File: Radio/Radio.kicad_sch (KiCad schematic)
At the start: 22 parts, among them SW1 Bourns PEC11R, SW2 Bourns PEC11R, SW3 SW_Push, SW4 SW_Push, U1 LM386, U2 RDA5807M_Module

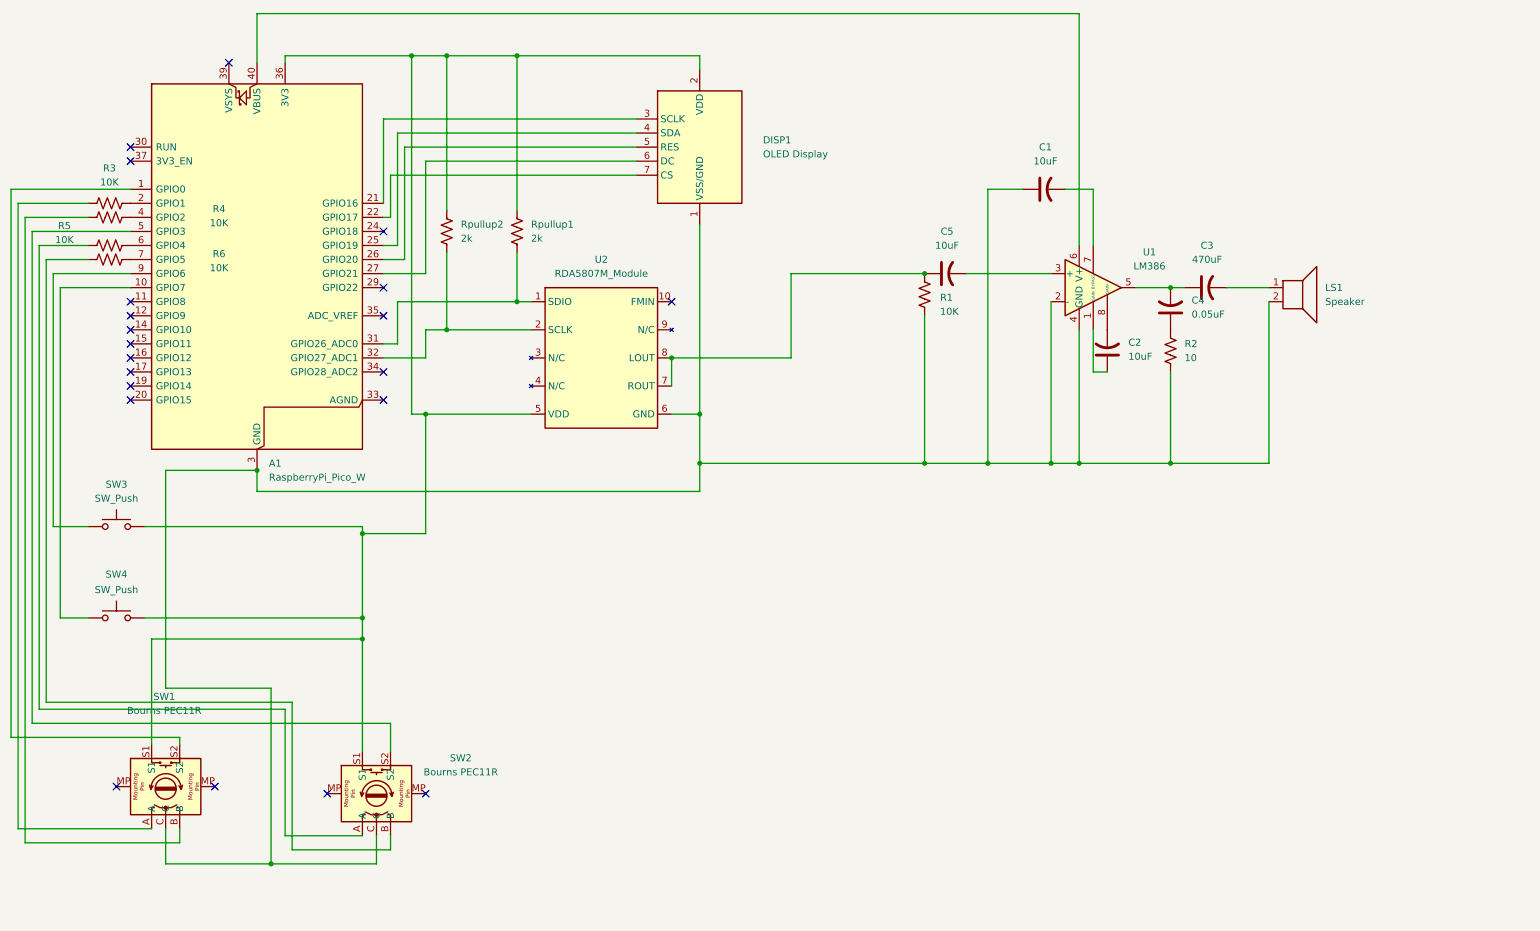
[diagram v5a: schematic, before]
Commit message: updated PCB with filters
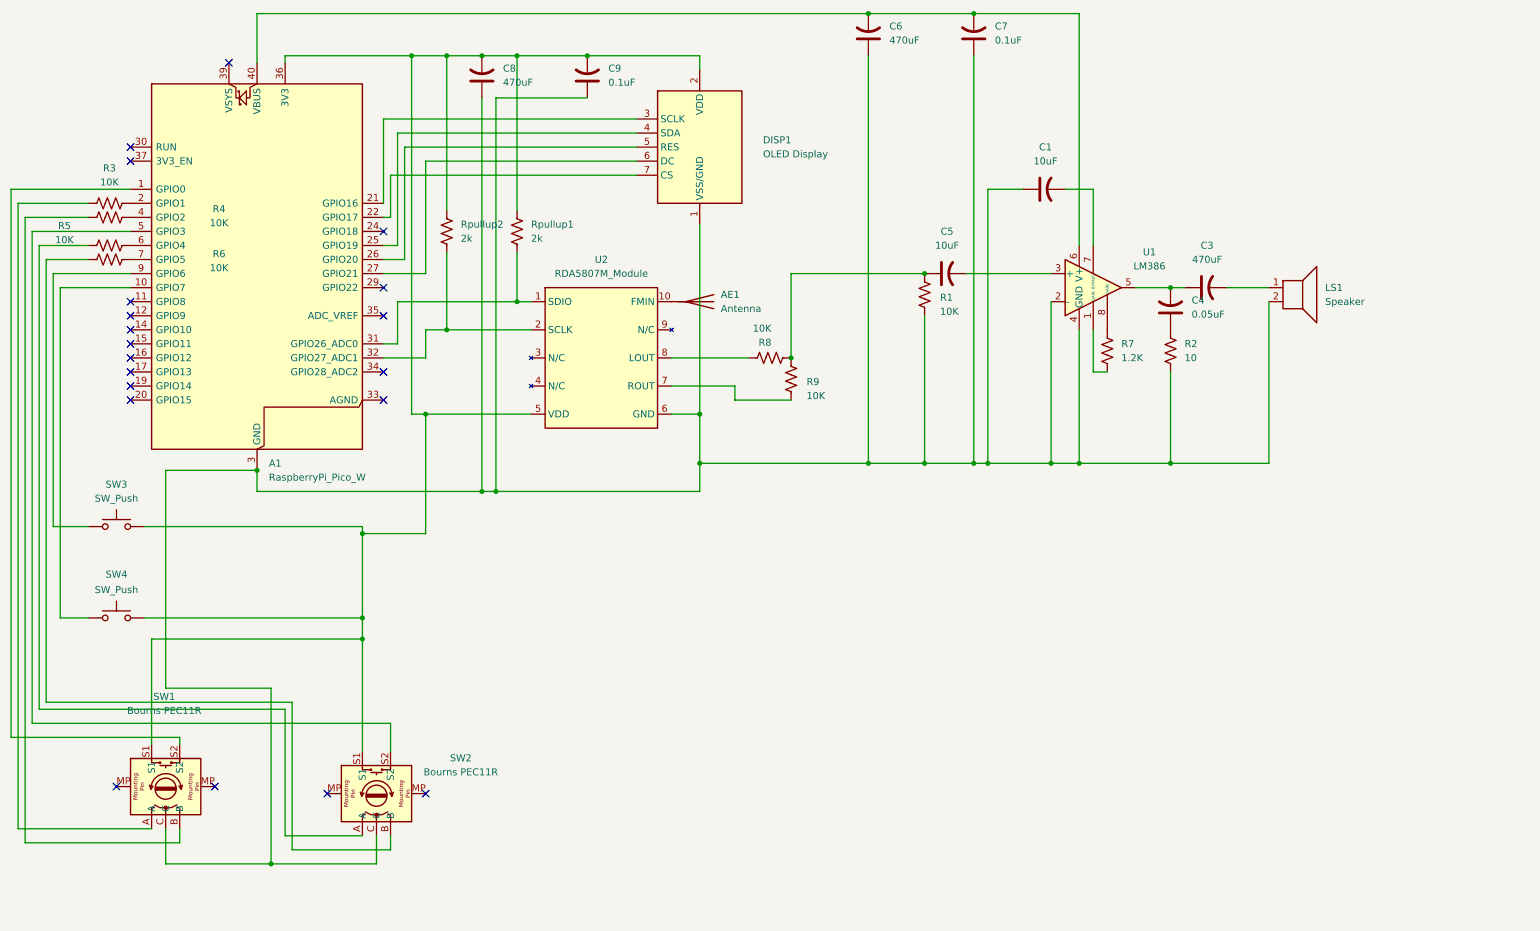
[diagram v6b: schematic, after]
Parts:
- removed C2: 10uF, Capacitor_THT:C_Rect_L4.0mm_W2.5mm_P2.50mm, symbol Device:C_US
- added AE1: Antenna, symbol Device:Antenna
- added C6, C8: 470uF, Capacitor_THT:C_Rect_L4.0mm_W2.5mm_P2.50mm, symbol Device:C_US
- added C7, C9: 0.1uF, Capacitor_THT:C_Rect_L4.0mm_W2.5mm_P2.50mm, symbol Device:C_US
- added R7: 1.2K, Resistor_THT:R_Axial_DIN0204_L3.6mm_D1.6mm_P5.08mm_Horizontal, symbol Device:R_US
- added R8, R9: 10K, Resistor_THT:R_Axial_DIN0204_L3.6mm_D1.6mm_P5.08mm_Horizontal, symbol Device:R_US
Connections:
- net at A1.36 (3V3), DISP1.2 (VDD), Rpullup1.1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: now also C8.2, C9.2
- net at U1.1 (GAIN): now also R7.1
- net at U1.8 (GAIN): now also R7.2
- net at A1.13 (GND), A1.18 (GND), A1.23 (GND)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: now also C6.1, C7.1, C8.1, C9.1
- net at A1.40 (VBUS), U1.6 (V+): now also C6.2, C7.2
- net at C5.1, R1.2: now also R8.1, R9.2; no longer U2.7 (ROUT), U2.8 (LOUT)
- net at U2.10 (FMIN): now also AE1.1 (A)
- new net: R8.2, U2.8 (LOUT)
- new net: R9.1, U2.7 (ROUT)
- no-connect marks 21 -> 20

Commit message: Made PCB and moved a few gpio pins for buttons
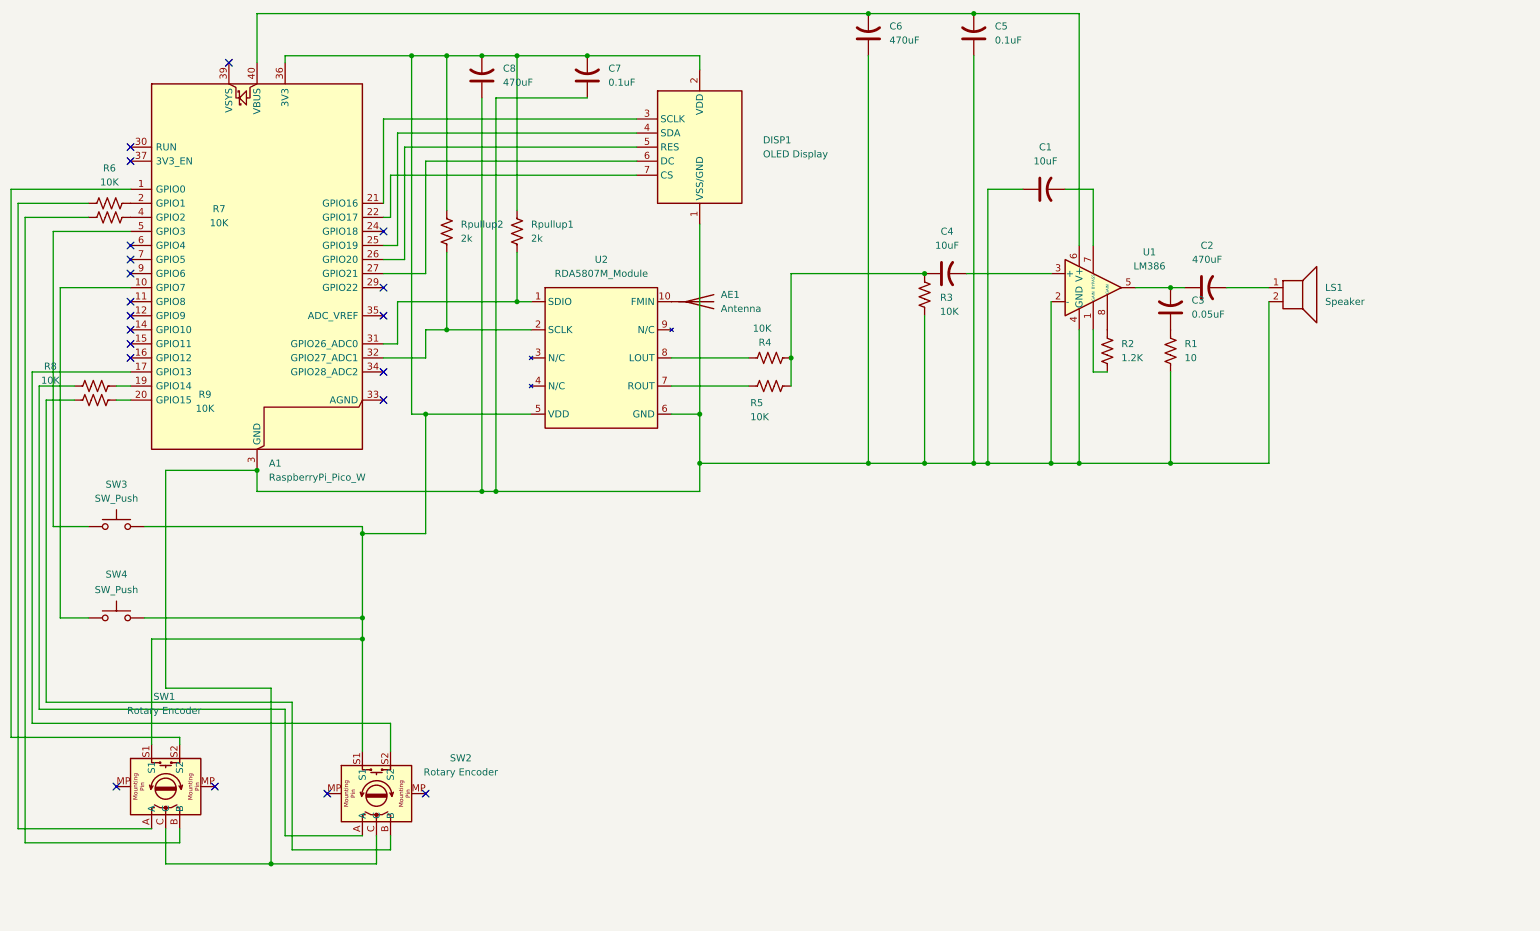
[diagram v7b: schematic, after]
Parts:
- A1: footprint Module:RaspberryPi_Pico_W_SMD_HandSolder -> ECE:RPi_Pico_TH
- AE1: footprint (none) -> TestPoint:TestPoint_Pad_D1.0mm
- C1, C6, C8: footprint Capacitor_THT:C_Rect_L4.0mm_W2.5mm_P2.50mm -> Capacitor_THT:CP_Radial_D6.3mm_P2.50mm
- C2: renamed from C3; footprint Capacitor_THT:C_Rect_L4.0mm_W2.5mm_P2.50mm -> Capacitor_THT:CP_Radial_D6.3mm_P2.50mm
- C3: renamed from C4; footprint Capacitor_THT:C_Rect_L4.0mm_W2.5mm_P2.50mm -> Capacitor_THT:C_Disc_D3.0mm_W1.6mm_P2.50mm
- C4: renamed from C5; footprint Capacitor_THT:C_Rect_L4.0mm_W2.5mm_P2.50mm -> Capacitor_THT:CP_Radial_D6.3mm_P2.50mm
- C5: renamed from C7; footprint Capacitor_THT:C_Rect_L4.0mm_W2.5mm_P2.50mm -> Capacitor_THT:C_Disc_D3.0mm_W1.6mm_P2.50mm
- C7: renamed from C9; footprint Capacitor_THT:C_Rect_L4.0mm_W2.5mm_P2.50mm -> Capacitor_THT:C_Disc_D3.0mm_W1.6mm_P2.50mm
- LS1: footprint Buzzer_Beeper:Speaker_CUI_CMR-1206S-67 -> TerminalBlock_Phoenix:TerminalBlock_Phoenix_MKDS-1,5-2_1x02_P5.00mm_Horizontal
- R1: renamed from R2; footprint Resistor_THT:R_Axial_DIN0204_L3.6mm_D1.6mm_P5.08mm_Horizontal -> Resistor_THT:R_Axial_DIN0207_L6.3mm_D2.5mm_P10.16mm_Horizontal
- R2: renamed from R7; footprint Resistor_THT:R_Axial_DIN0204_L3.6mm_D1.6mm_P5.08mm_Horizontal -> Resistor_THT:R_Axial_DIN0207_L6.3mm_D2.5mm_P10.16mm_Horizontal
- R3: renamed from R1; footprint Resistor_THT:R_Axial_DIN0204_L3.6mm_D1.6mm_P5.08mm_Horizontal -> Resistor_THT:R_Axial_DIN0207_L6.3mm_D2.5mm_P10.16mm_Horizontal
- R4: renamed from R8; footprint Resistor_THT:R_Axial_DIN0204_L3.6mm_D1.6mm_P5.08mm_Horizontal -> Resistor_THT:R_Axial_DIN0207_L6.3mm_D2.5mm_P10.16mm_Horizontal
- R5: renamed from R9; footprint Resistor_THT:R_Axial_DIN0204_L3.6mm_D1.6mm_P5.08mm_Horizontal -> Resistor_THT:R_Axial_DIN0207_L6.3mm_D2.5mm_P10.16mm_Horizontal
- R6: renamed from R3; footprint Resistor_THT:R_Axial_DIN0204_L3.6mm_D1.6mm_P5.08mm_Horizontal -> Resistor_THT:R_Axial_DIN0207_L6.3mm_D2.5mm_P10.16mm_Horizontal
- R7: renamed from R4; footprint Resistor_THT:R_Axial_DIN0204_L3.6mm_D1.6mm_P5.08mm_Horizontal -> Resistor_THT:R_Axial_DIN0207_L6.3mm_D2.5mm_P10.16mm_Horizontal
- R8: renamed from R5; footprint Resistor_THT:R_Axial_DIN0204_L3.6mm_D1.6mm_P5.08mm_Horizontal -> Resistor_THT:R_Axial_DIN0207_L6.3mm_D2.5mm_P10.16mm_Horizontal
- R9: renamed from R6; footprint Resistor_THT:R_Axial_DIN0204_L3.6mm_D1.6mm_P5.08mm_Horizontal -> Resistor_THT:R_Axial_DIN0207_L6.3mm_D2.5mm_P10.16mm_Horizontal
- Rpullup1, Rpullup2: footprint Resistor_THT:R_Axial_DIN0204_L3.6mm_D1.6mm_P5.08mm_Horizontal -> Resistor_THT:R_Axial_DIN0207_L6.3mm_D2.5mm_P10.16mm_Horizontal
- SW1, SW2: value Bourns PEC11R -> Rotary Encoder
- U1: footprint Package_DIP:DIP-8_W7.62mm_Socket -> Package_DIP:DIP-8_W7.62mm
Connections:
- net at SW3.1: now also A1.5 (GPIO3); no longer A1.9 (GPIO6)
- net at R9.2: now also A1.20 (GPIO15); no longer A1.7 (GPIO5)
- net at R8.2: now also A1.19 (GPIO14); no longer A1.6 (GPIO4)
- net at SW2.S2: now also A1.17 (GPIO13); no longer A1.5 (GPIO3)
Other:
- moved on the sheet: R5, R8, R9
